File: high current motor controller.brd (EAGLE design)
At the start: 100 x 80 mm, 51 parts, among them IC1 LM2676S, Q1 IPT004N03L, Q2 IPT004N03L, Q3 IPT004N03L, Q4 IPT004N03L

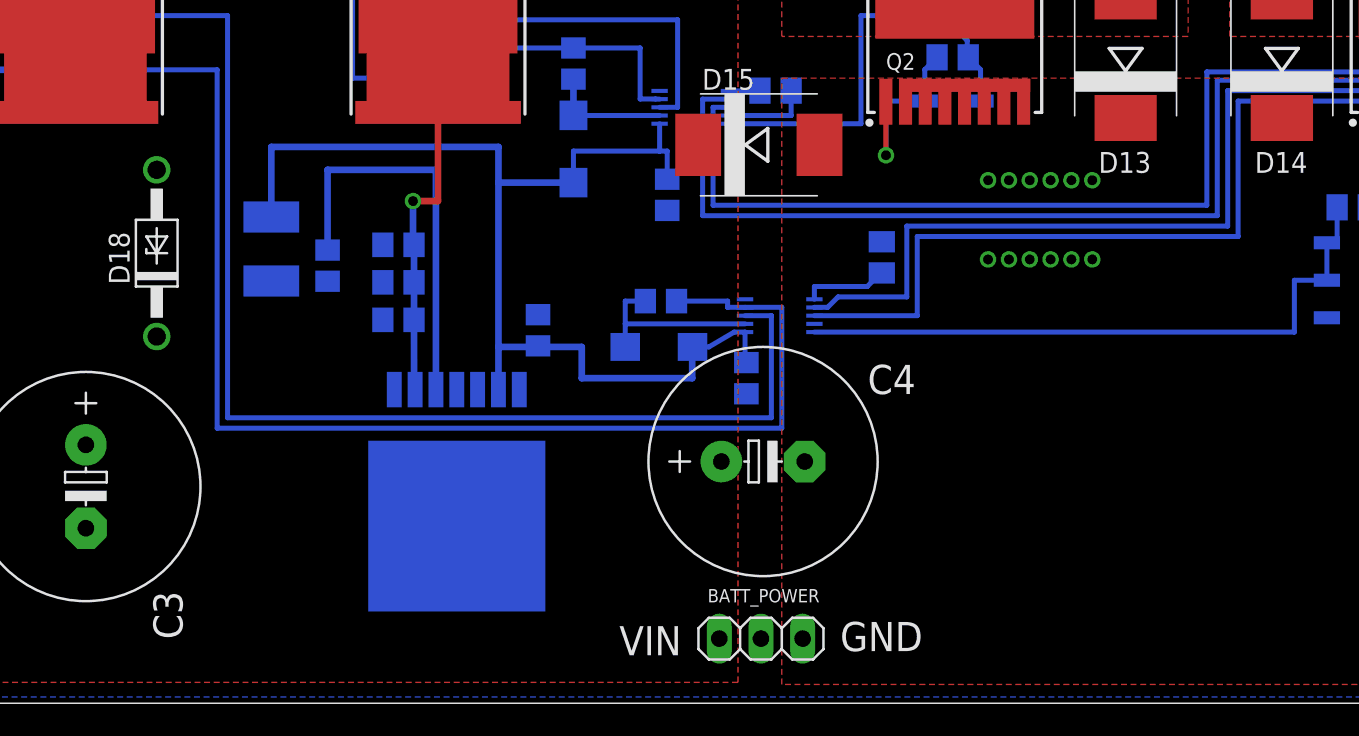
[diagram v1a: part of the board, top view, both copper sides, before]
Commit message: Fixed regulator layout. TODO:Select values for regulator components
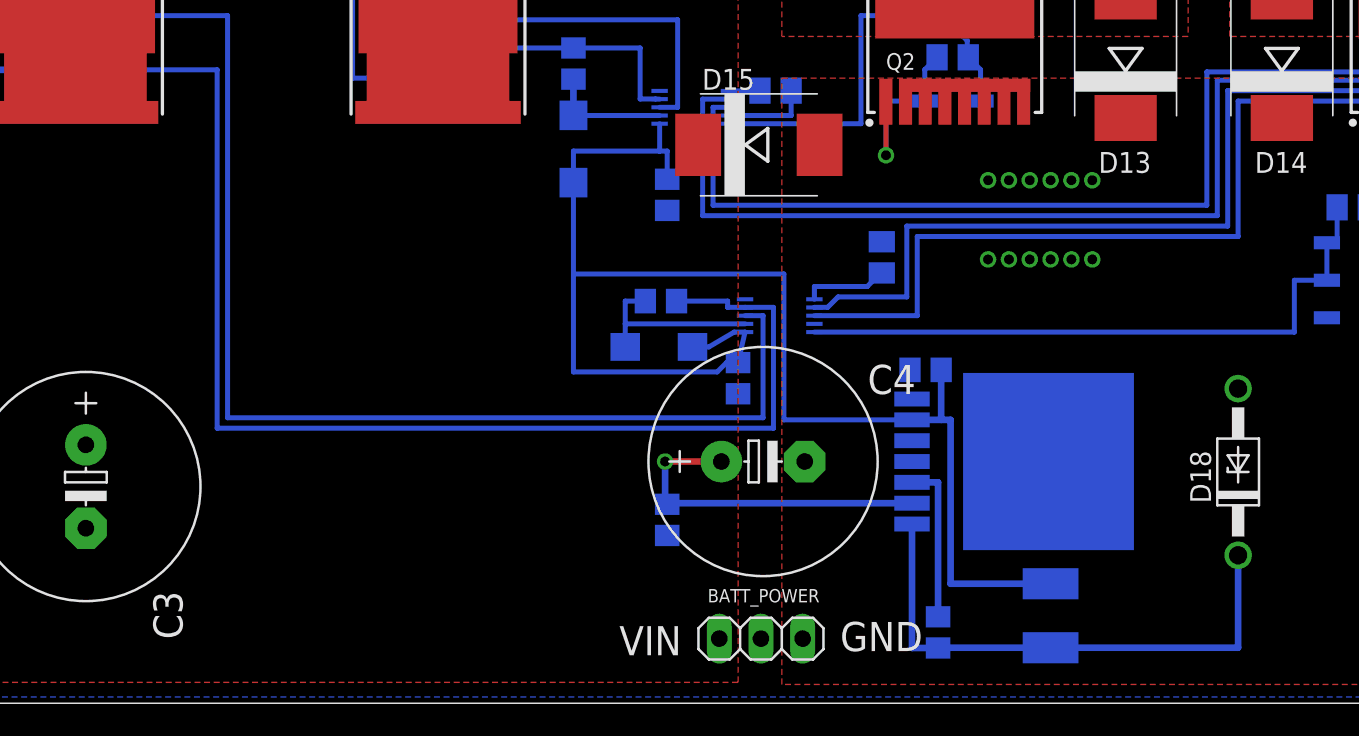
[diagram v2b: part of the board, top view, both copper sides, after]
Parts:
- removed C10: 15u, resistor:C0805
- removed C9: 0.47u, resistor:C0805
- C11: value 15u -> 100u
- moved D18 67.2 mm to (79.2, 14.1)
- moved L1 52.5 mm to (67.8, 5.33)
- moved C13 43.4 mm to (61.0, 4.32)
- moved IC1 33.6 mm to (65.2, 14.7), turned to 90 degrees
- moved C12 23.7 mm to (60.2, 20.3), turned to 0 degrees
- moved C11 23.4 mm to (44.5, 11.2), turned to 270 degrees
- moved C8 0.51 mm to (48.8, 19.8)
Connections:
- net GND: no longer C10.2, C9.2
- net VIN: no longer C10.1, C9.1
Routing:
- net N$17: track 0.00 -> 33.1 mm
- net 12V: track 69.5 -> 89.2 mm
- net N$16: track 24.9 -> 9.78 mm
- net VIN: track 19.2 -> 21.1 mm
- net BHS: track 103.5 -> 102.5 mm
- net BHO: track 79.2 -> 78.2 mm
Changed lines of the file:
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@@
 <attribute name="VALUE" x="42.799" y="27.051" size="1.27" layer="28" rot="MR180"/>
 </element>
-<element name="C8" library="resistor" package="C0805" value="" x="49.276" y="19.812" smashed="yes" rot="MR270">
-<attribute name="NAME" x="50.8" y="18.542" size="1.27" layer="26" rot="MR180"/>
-<attribute name="VALUE" x="51.816" y="21.082" size="1.27" layer="28" rot="MR270"/>
+<element name="C8" library="resistor" package="C0805" value="" x="48.768" y="19.812" smashed="yes" rot="MR270">
+<attribute name="NAME" x="50.292" y="18.542" size="1.27" layer="26" rot="MR180"/>
+<attribute name="VALUE" x="51.308" y="21.082" size="1.27" layer="28" rot="MR270"/>
 </element>
 <element name="D1" library="semicon-smd-ipc" package="SOD123" value="" x="30.988" y="39.243" smashed="yes" rot="MR0">
@@
 <attribute name="VALUE" x="46.355" y="0.762" size="1.27" layer="27"/>
 </element>
-<element name="IC1" library="v-reg-3" package="TO263-7" value="LM2676S" x="31.623" y="13.335" rot="MR180"/>
-<element name="C9" library="resistor" package="C0805" value="0.47u" x="28.067" y="23.368" rot="MR0"/>
-<element name="C10" library="resistor" package="C0805" value="15u" x="28.067" y="25.654" rot="MR0"/>
-<element name="C11" library="resistor" package="C0805" value="15u" x="28.067" y="27.94" rot="MR0"/>
-<element name="C12" library="resistor" package="C0805" value="180u" x="36.576" y="22.733" rot="MR90"/>
-<element name="C13" library="resistor" package="C0805" value="0.01u" x="23.749" y="26.67" rot="MR270"/>
-<element name="L1" library="resistor" package="L1812" value="33u" x="20.32" y="27.686" rot="MR90"/>
-<element name="D18" library="diode" package="DO41Z10" value="1N4728" x="13.335" y="27.432" rot="R90"/>
+<element name="IC1" library="v-reg-3" package="TO263-7" value="LM2676S" x="65.151" y="14.732" rot="MR90"/>
+<element name="C11" library="resistor" package="C0805" value="100u" x="44.45" y="11.176" rot="MR270"/>
+<element name="C12" library="resistor" package="C0805" value="180u" x="60.198" y="20.32" rot="MR0"/>
+<element name="C13" library="resistor" package="C0805" value="0.01u" x="60.96" y="4.318" rot="MR270"/>
+<element name="L1" library="resistor" package="L1812" value="33u" x="67.818" y="5.334" rot="MR90"/>
+<element name="D18" library="diode" package="DO41Z10" value="1N4728" x="79.248" y="14.097" rot="R90"/>
 </elements>
 <signals>
@@
 <wire x1="8.321" y1="44.323" x2="7.19" y2="45.454" width="0.4064" layer="16"/>
 <wire x1="7.19" y1="45.454" x2="7.19" y2="46.863" width="0.4064" layer="16"/>
-<wire x1="49.1949" y1="23.622" x2="50.8" y2="23.622" width="0.3048" layer="16"/>
-<wire x1="50.8" y1="23.622" x2="50.8" y2="17.399" width="0.3048" layer="16"/>
-<wire x1="50.8" y1="17.399" x2="17.653" y2="17.399" width="0.3048" layer="16"/>
+<wire x1="49.1949" y1="23.622" x2="50.292" y2="23.622" width="0.3048" layer="16"/>
+<wire x1="50.292" y1="23.622" x2="50.292" y2="17.399" width="0.3048" layer="16"/>
+<wire x1="50.292" y1="17.399" x2="17.653" y2="17.399" width="0.3048" layer="16"/>
 <wire x1="17.653" y1="17.399" x2="17.653" y2="41.91" width="0.3048" layer="16"/>
 <wire x1="17.653" y1="41.91" x2="10.463" y2="41.91" width="0.3048" layer="16"/>
@@
 <wire x1="10.463" y1="38.608" x2="17.018" y2="38.608" width="0.3048" layer="16"/>
 <wire x1="17.018" y1="38.608" x2="17.018" y2="16.764" width="0.3048" layer="16"/>
-<wire x1="17.018" y1="16.764" x2="51.435" y2="16.764" width="0.3048" layer="16"/>
-<wire x1="51.435" y1="16.764" x2="51.435" y2="24.13" width="0.3048" layer="16"/>
-<wire x1="51.435" y1="24.13" x2="49.1949" y2="24.13" width="0.3048" layer="16"/>
+<wire x1="17.018" y1="16.764" x2="50.927" y2="16.764" width="0.3048" layer="16"/>
+<wire x1="50.927" y1="16.764" x2="50.927" y2="24.13" width="0.3048" layer="16"/>
+<wire x1="50.927" y1="24.13" x2="49.1949" y2="24.13" width="0.3048" layer="16"/>
 <wire x1="49.1949" y1="24.13" x2="49.1949" y2="24.122" width="0.3048" layer="16"/>
 </signal>
@@
 <contactref element="C11" pad="2"/>
 <contactref element="IC1" pad="4"/>
-<contactref element="C10" pad="2"/>
-<contactref element="C9" pad="2"/>
 <contactref element="C12" pad="2"/>
 <contactref element="D18" pad="A"/>
-<wire x1="49.276" y1="18.862" x2="52.832" y2="14.732" width="0" layer="19" extent="16-16"/>
 <wire x1="88.44" y1="36.66" x2="81.915" y2="35.67" width="0" layer="19" extent="1-1"/>
 </signal>
@@
 <contactref element="C8" pad="1"/>
 <contactref element="D17" pad="A"/>
-<wire x1="49.276" y1="20.762" x2="49.1949" y2="20.955" width="0.3048" layer="16"/>
-<wire x1="49.1949" y1="20.955" x2="49.1949" y2="22.622" width="0.3048" layer="16"/>
 <wire x1="49.1949" y1="22.622" x2="48.532" y2="22.622" width="0.3048" layer="16"/>
 <wire x1="48.532" y1="22.622" x2="46.99" y2="21.717" width="0.3048" layer="16"/>
@@
 <contactref element="C12" pad="1"/>
 <contactref element="IC1" pad="6"/>
-<wire x1="20.32" y1="29.636" x2="20.32" y2="33.909" width="0.4064" layer="16"/>
-<wire x1="20.32" y1="33.909" x2="34.163" y2="33.909" width="0.4064" layer="16"/>
-<wire x1="34.163" y1="31.732" x2="34.163" y2="21.717" width="0.4064" layer="16"/>
-<wire x1="34.163" y1="21.717" x2="34.163" y2="19.115" width="0.4064" layer="16"/>
-<wire x1="34.163" y1="33.909" x2="34.163" y2="31.732" width="0.4064" layer="16"/>
-<wire x1="34.163" y1="31.732" x2="38.735" y2="31.732" width="0.4064" layer="16"/>
-<wire x1="36.576" y1="21.717" x2="34.163" y2="21.717" width="0.4064" layer="16"/>
-<wire x1="36.576" y1="21.783" x2="36.576" y2="21.717" width="0.4064" layer="16"/>
-<wire x1="36.576" y1="21.717" x2="39.243" y2="21.717" width="0.4064" layer="16"/>
-<wire x1="39.243" y1="21.717" x2="39.243" y2="19.812" width="0.4064" layer="16"/>
-<wire x1="39.243" y1="19.812" x2="45.974" y2="19.812" width="0.4064" layer="16"/>
-<wire x1="45.974" y1="19.812" x2="45.974" y2="21.717" width="0.4064" layer="16"/>
-<wire x1="45.974" y1="21.717" x2="45.992" y2="21.717" width="0.4064" layer="16"/>
+<wire x1="59.371" y1="17.272" x2="61.148" y2="17.272" width="0.4064" layer="16"/>
+<wire x1="61.148" y1="17.272" x2="61.148" y2="20.32" width="0.4064" layer="16"/>
+<wire x1="48.768" y1="20.762" x2="48.067" y2="20.762" width="0.3048" layer="16"/>
+<wire x1="48.067" y1="20.762" x2="47.498" y2="20.193" width="0.3048" layer="16"/>
+<wire x1="47.498" y1="20.193" x2="38.735" y2="20.193" width="0.3048" layer="16"/>
+<wire x1="38.735" y1="20.193" x2="38.735" y2="26.162" width="0.3048" layer="16"/>
+<wire x1="38.735" y1="26.162" x2="38.735" y2="31.732" width="0.3048" layer="16"/>
+<wire x1="48.768" y1="20.762" x2="49.1949" y2="22.622" width="0.3048" layer="16"/>
+<wire x1="59.371" y1="17.272" x2="51.562" y2="17.272" width="0.3048" layer="16"/>
+<wire x1="51.562" y1="17.272" x2="51.562" y2="26.162" width="0.3048" layer="16"/>
+<wire x1="51.562" y1="26.162" x2="38.735" y2="26.162" width="0.3048" layer="16"/>
+<wire x1="67.818" y1="7.284" x2="61.722" y2="7.284" width="0.4064" layer="16"/>
+<wire x1="61.722" y1="7.284" x2="61.722" y2="17.272" width="0.4064" layer="16"/>
+<wire x1="61.722" y1="17.272" x2="61.148" y2="17.272" width="0.4064" layer="16"/>
 </signal>
 <signal name="N$3">
@@
 <contactref element="IC1" pad="2"/>
 <contactref element="C11" pad="1"/>
-<contactref element="C10" pad="1"/>
-<contactref element="C9" pad="1"/>
-<wire x1="29.083" y1="19.115" x2="29.022" y2="19.115" width="0.4064" layer="16"/>
-<wire x1="29.022" y1="19.115" x2="29.017" y2="23.368" width="0.4064" layer="16"/>
-<wire x1="29.017" y1="23.368" x2="29.017" y2="25.654" width="0.4064" layer="16"/>
-<wire x1="29.017" y1="25.654" x2="29.017" y2="27.94" width="0.4064" layer="16"/>
-<wire x1="29.017" y1="27.94" x2="28.956" y2="27.94" width="0.4064" layer="16"/>
-<wire x1="28.956" y1="27.94" x2="28.956" y2="30.607" width="0.4064" layer="16"/>
-<via x="28.956" y="30.607" extent="1-16" drill="0.6"/>
-<wire x1="28.956" y1="30.607" x2="30.48" y2="30.607" width="0.4064" layer="1"/>
-<wire x1="30.48" y1="30.607" x2="30.48" y2="36.66" width="0.4064" layer="1"/>
+<wire x1="59.371" y1="12.192" x2="44.45" y2="12.192" width="0.4064" layer="16"/>
+<wire x1="44.45" y1="12.192" x2="44.45" y2="12.126" width="0.4064" layer="16"/>
+<wire x1="44.45" y1="12.126" x2="44.323" y2="12.126" width="0.4064" layer="16"/>
+<wire x1="44.323" y1="12.126" x2="44.323" y2="14.732" width="0.4064" layer="16"/>
+<via x="44.323" y="14.732" extent="1-16" drill="0.6"/>
+<wire x1="44.323" y1="14.732" x2="47.752" y2="14.732" width="0.4064" layer="1"/>
 </signal>
 <signal name="N$16">
 <contactref element="IC1" pad="3"/>
 <contactref element="C13" pad="1"/>
-<wire x1="30.353" y1="19.115" x2="30.353" y2="32.512" width="0.4064" layer="16"/>
-<wire x1="30.353" y1="32.512" x2="23.749" y2="32.512" width="0.4064" layer="16"/>
-<wire x1="23.749" y1="32.512" x2="23.749" y2="27.62" width="0.4064" layer="16"/>
+<wire x1="59.371" y1="13.462" x2="60.96" y2="13.462" width="0.4064" layer="16"/>
+<wire x1="60.96" y1="13.462" x2="60.96" y2="5.268" width="0.4064" layer="16"/>
 </signal>
 <signal name="N$17">
@@
 <contactref element="D18" pad="C"/>
 <contactref element="C13" pad="2"/>
-<wire x1="20.32" y1="25.736" x2="23.749" y2="25.72" width="0" layer="19" extent="16-16"/>
-<wire x1="27.813" y1="19.115" x2="23.749" y2="25.72" width="0" layer="19" extent="16-16"/>
-<wire x1="13.335" y1="22.352" x2="20.32" y2="25.736" width="0" layer="19" extent="16-16"/>
+<wire x1="59.371" y1="10.922" x2="59.371" y2="3.368" width="0.4064" layer="16"/>
+<wire x1="59.371" y1="3.368" x2="60.96" y2="3.368" width="0.4064" layer="16"/>
+<wire x1="60.96" y1="3.368" x2="60.96" y2="3.384" width="0.4064" layer="16"/>
+<wire x1="60.96" y1="3.384" x2="67.818" y2="3.384" width="0.4064" layer="16"/>
+<wire x1="67.818" y1="3.384" x2="79.248" y2="3.384" width="0.4064" layer="16"/>
+<wire x1="79.248" y1="3.384" x2="79.248" y2="9.017" width="0.4064" layer="16"/>
 </signal>
 </signals>

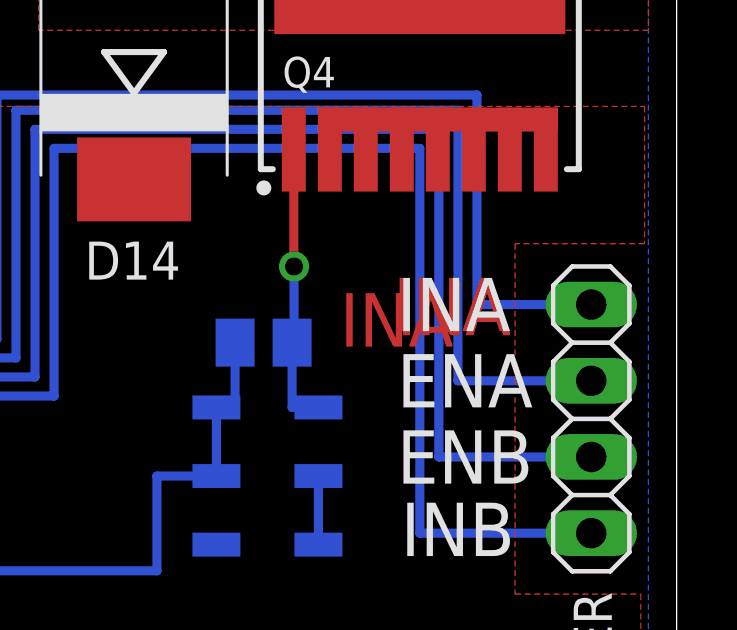
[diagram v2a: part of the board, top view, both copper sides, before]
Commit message: Fixed silk screen overlap errors and selected values for regulator components TODO:Find corrent footprints for regulator components
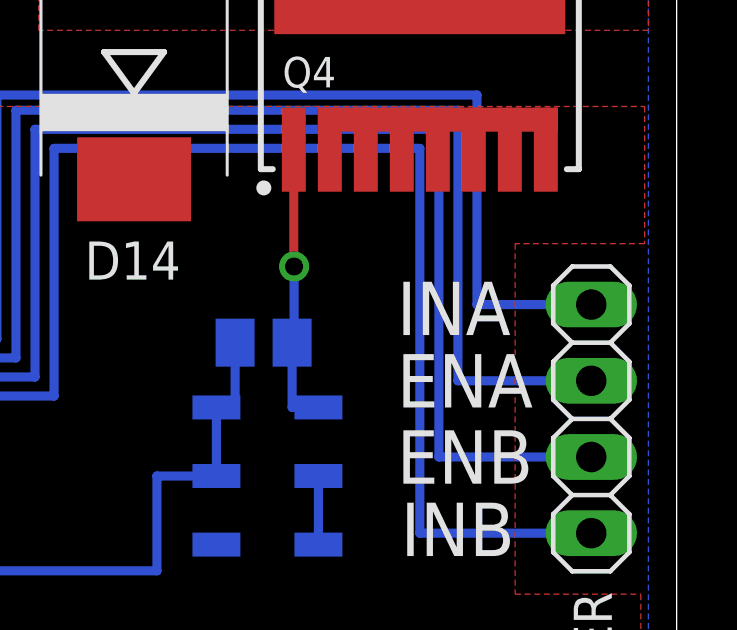
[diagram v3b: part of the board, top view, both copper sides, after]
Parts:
- C11: value 100u -> 30u
- C12: value 180u -> 100u
- L1: value 33u -> 68u
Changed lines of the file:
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@@
 <wire x1="100" y1="80" x2="0" y2="80" width="0" layer="20"/>
 <wire x1="0" y1="80" x2="0" y2="0" width="0" layer="20"/>
-<text x="90.551" y="30.607" size="1.778" layer="1">INA</text>
-<text x="90.678" y="30.48" size="1.778" layer="1">INA</text>
-<text x="90.678" y="30.48" size="1.778" layer="1">INA</text>
-<text x="90.678" y="30.48" size="1.778" layer="1">INA</text>
-<text x="90.678" y="30.48" size="1.778" layer="1">INA</text>
-<text x="88.773" y="30.099" size="1.778" layer="1">INA</text>
-<text x="90.678" y="30.607" size="1.778" layer="121">INA</text>
+<text x="90.678" y="30.48" size="1.778" layer="121">INA</text>
 <text x="90.678" y="28.067" size="1.778" layer="121">ENA</text>
 <text x="90.678" y="25.527" size="1.778" layer="121">ENB</text>
@@
 <attribute name="VALUE" x="46.355" y="0.762" size="1.27" layer="27"/>
 </element>
-<element name="IC1" library="v-reg-3" package="TO263-7" value="LM2676S" x="65.151" y="14.732" rot="MR90"/>
-<element name="C11" library="resistor" package="C0805" value="100u" x="44.45" y="11.176" rot="MR270"/>
-<element name="C12" library="resistor" package="C0805" value="180u" x="60.198" y="20.32" rot="MR0"/>
-<element name="C13" library="resistor" package="C0805" value="0.01u" x="60.96" y="4.318" rot="MR270"/>
-<element name="L1" library="resistor" package="L1812" value="33u" x="67.818" y="5.334" rot="MR90"/>
+<element name="IC1" library="v-reg-3" package="TO263-7" value="LM2676S" x="65.151" y="14.732" smashed="yes" rot="MR90">
+<attribute name="NAME" x="72.644" y="20.701" size="1.27" layer="26" rot="MR0"/>
+<attribute name="VALUE" x="69.215" y="20.701" size="0.8128" layer="28" rot="MR0"/>
+</element>
+<element name="C11" library="resistor" package="C0805" value="30u" x="44.45" y="11.176" smashed="yes" rot="MR270">
+<attribute name="NAME" x="42.926" y="12.446" size="1.27" layer="26" rot="MR270"/>
+</element>
+<element name="C12" library="resistor" package="C0805" value="100u" x="60.198" y="20.32" smashed="yes" rot="MR0">
+<attribute name="NAME" x="63.373" y="21.717" size="1.27" layer="26" rot="MR0"/>
+</element>
+<element name="C13" library="resistor" package="C0805" value="0.01u" x="60.96" y="4.318" smashed="yes" rot="MR270">
+<attribute name="NAME" x="62.484" y="6.096" size="1.27" layer="26" rot="MR180"/>
+</element>
+<element name="L1" library="resistor" package="L1812" value="68u" x="67.818" y="5.334" smashed="yes" rot="MR90">
+<attribute name="NAME" x="70.231" y="8.001" size="1.27" layer="26" rot="MR180"/>
+</element>
 <element name="D18" library="diode" package="DO41Z10" value="1N4728" x="79.248" y="14.097" rot="R90"/>
 </elements>
@@
 </signal>
 </signals>
+<errors>
+</errors>
 </board>
 </drawing>
